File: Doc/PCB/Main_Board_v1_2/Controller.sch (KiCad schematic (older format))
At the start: 74 parts, among them J10 BPM, J11 UART, J12 I2C Interface LCD_C, J13 BUZZER_C, J16 IP, J17 -, J18 BREATH, J19 EP, J20 +, J21 VOL_MIN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

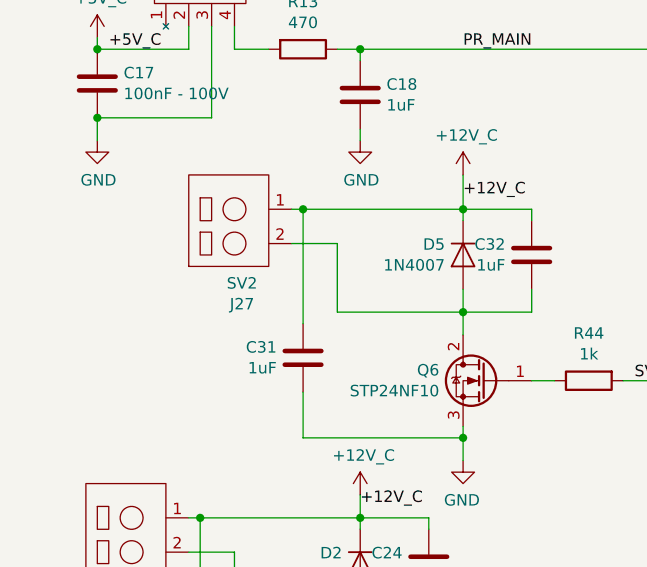
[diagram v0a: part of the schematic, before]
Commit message: Fixed SilkScreen V1.2 THT
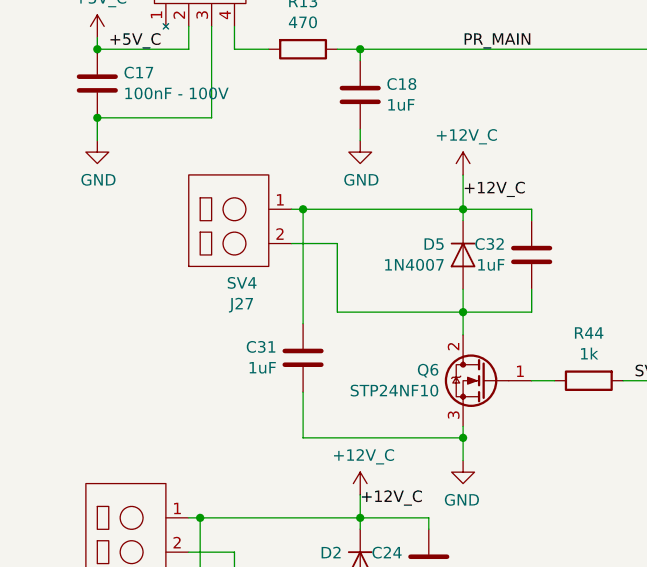
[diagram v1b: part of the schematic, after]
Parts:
- J27: value SV2 -> SV4
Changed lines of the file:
@@
 AR Path="/5E9339D0/5ED22175" Ref="J27"  Part="1"
 F 0 "J27" V 1765 3317 50  0000 C CNN
-F 1 "SV2" V 1674 3317 50  0000 C CNN
+F 1 "SV4" V 1674 3317 50  0000 C CNN
 F 2 "Ventilator:PinHeader_1x02_Screwless_3.5mm" H 1350 3700 50  0001 C CNN
 F 3 "https://es.rs-online.com/web/p/bloques-terminales-para-pcb/1232052/" H 1350 3700 50  0001 C CNN
